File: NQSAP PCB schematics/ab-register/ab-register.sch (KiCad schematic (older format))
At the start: 56 parts, among them J1 Bus, J2 Bus, J5 Conn_02x08, J6 Conn_02x08, U1 74LS377, U2 74LS245, U3 74LS377, U4 74LS245, U5 74LS138, U6 74LS138

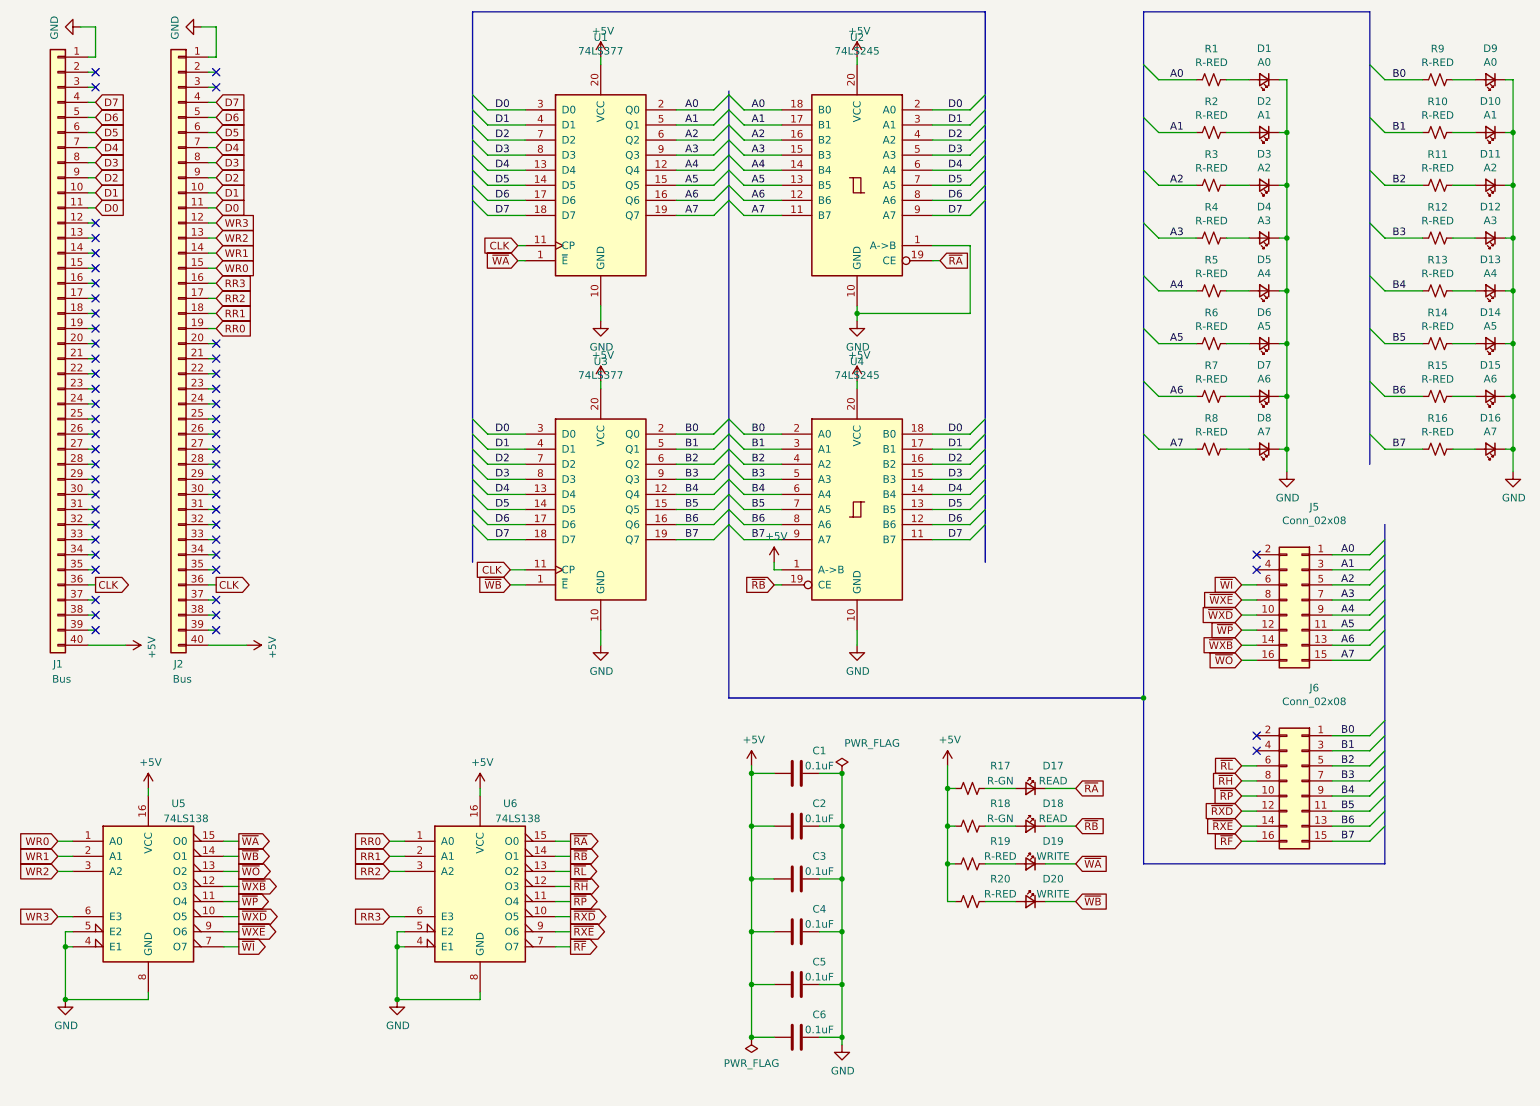
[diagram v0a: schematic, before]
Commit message: Add RAM, update and add gerbers for new boards
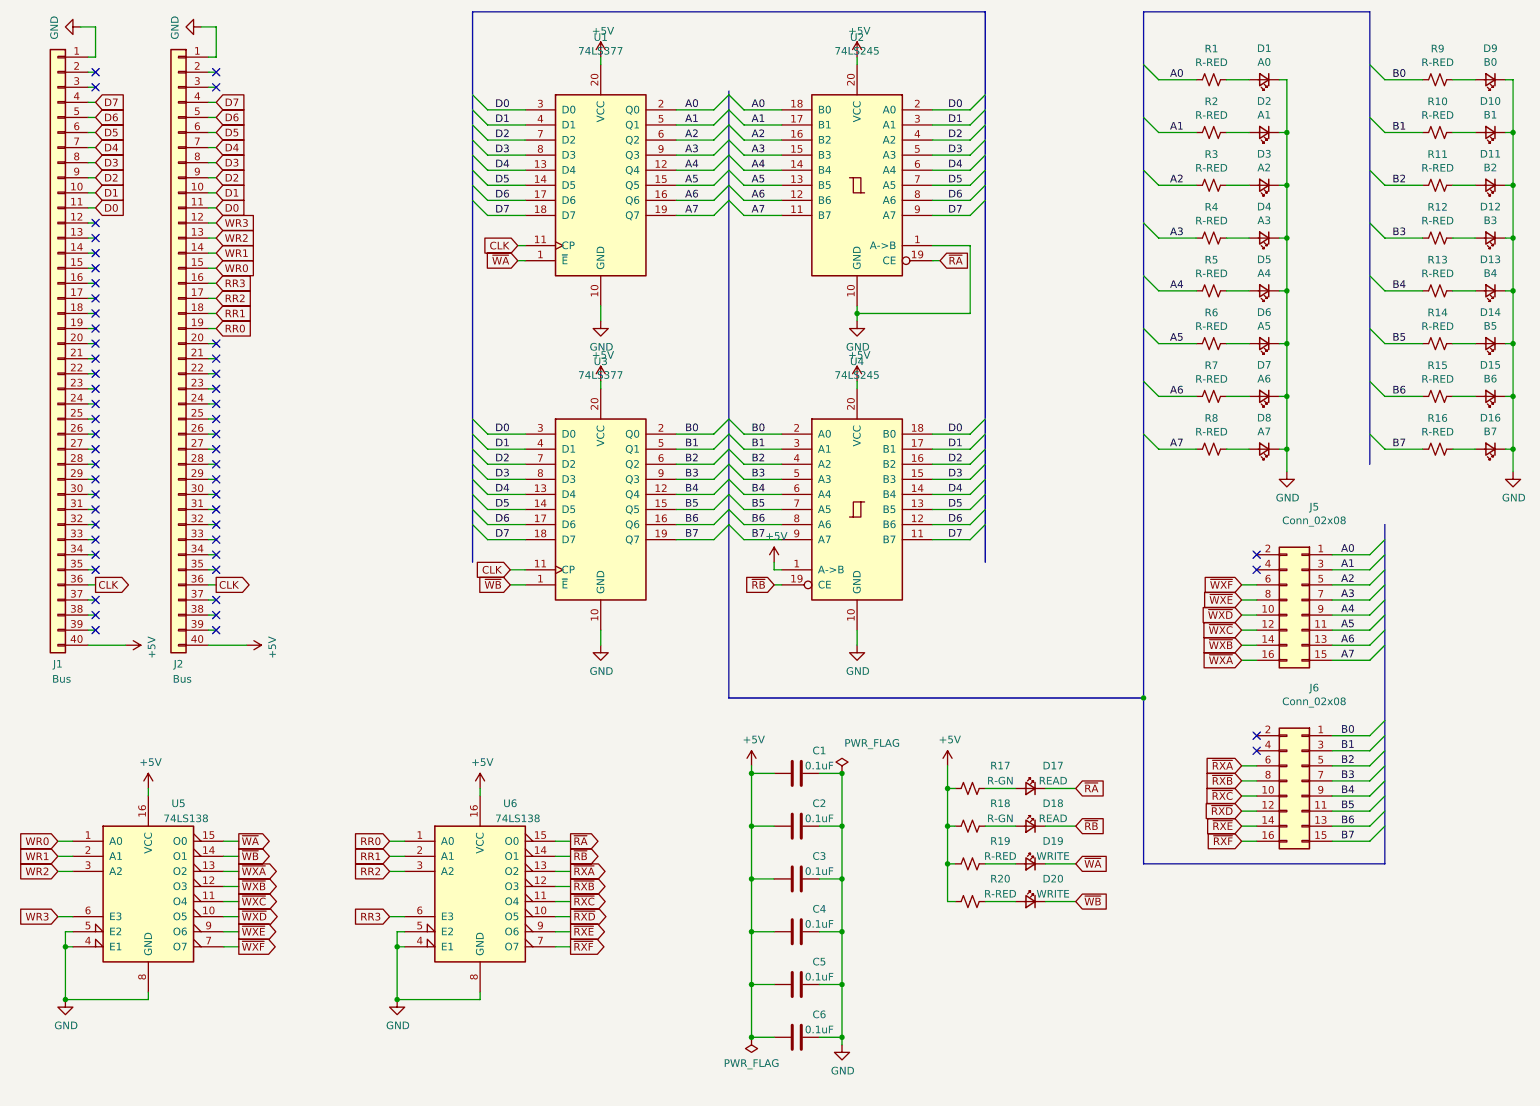
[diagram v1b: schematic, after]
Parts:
- D10: value A1 -> B1
- D11: value A2 -> B2
- D12: value A3 -> B3
- D13: value A4 -> B4
- D14: value A5 -> B5
- D15: value A6 -> B6
- D16: value A7 -> B7
- D9: value A0 -> B0
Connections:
- net ~RF renamed ~RXF
- net ~RH renamed ~RXB
- net ~RL renamed ~RXA
- net ~RP renamed ~RXC
- net ~WI renamed ~WXF
- net ~WO renamed ~WXA
- net ~WP renamed ~WXC
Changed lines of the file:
@@
 P 10300 1050
 F 0 "D9" H 10300 843 50  0000 C CNN
-F 1 "A0" H 10300 934 50  0000 C CNN
+F 1 "B0" H 10300 934 50  0000 C CNN
 F 2 "LED_SMD:LED_0805_2012Metric_Pad1.15x1.40mm_HandSolder" V 10300 1050 50  0001 C CNN
 F 3 "~" V 10300 1050 50  0001 C CNN
@@
 P 10300 1400
 F 0 "D10" H 10300 1193 50  0000 C CNN
-F 1 "A1" H 10300 1284 50  0000 C CNN
+F 1 "B1" H 10300 1284 50  0000 C CNN
 F 2 "LED_SMD:LED_0805_2012Metric_Pad1.15x1.40mm_HandSolder" V 10300 1400 50  0001 C CNN
 F 3 "~" V 10300 1400 50  0001 C CNN
@@
 P 10300 1750
 F 0 "D11" H 10300 1543 50  0000 C CNN
-F 1 "A2" H 10300 1634 50  0000 C CNN
+F 1 "B2" H 10300 1634 50  0000 C CNN
 F 2 "LED_SMD:LED_0805_2012Metric_Pad1.15x1.40mm_HandSolder" V 10300 1750 50  0001 C CNN
 F 3 "~" V 10300 1750 50  0001 C CNN
@@
 P 10300 2100
 F 0 "D12" H 10300 1893 50  0000 C CNN
-F 1 "A3" H 10300 1984 50  0000 C CNN
+F 1 "B3" H 10300 1984 50  0000 C CNN
 F 2 "LED_SMD:LED_0805_2012Metric_Pad1.15x1.40mm_HandSolder" V 10300 2100 50  0001 C CNN
 F 3 "~" V 10300 2100 50  0001 C CNN
@@
 P 10300 2450
 F 0 "D13" H 10300 2243 50  0000 C CNN
-F 1 "A4" H 10300 2334 50  0000 C CNN
+F 1 "B4" H 10300 2334 50  0000 C CNN
 F 2 "LED_SMD:LED_0805_2012Metric_Pad1.15x1.40mm_HandSolder" V 10300 2450 50  0001 C CNN
 F 3 "~" V 10300 2450 50  0001 C CNN
@@
 P 10300 2800
 F 0 "D14" H 10300 2593 50  0000 C CNN
-F 1 "A5" H 10300 2684 50  0000 C CNN
+F 1 "B5" H 10300 2684 50  0000 C CNN
 F 2 "LED_SMD:LED_0805_2012Metric_Pad1.15x1.40mm_HandSolder" V 10300 2800 50  0001 C CNN
 F 3 "~" V 10300 2800 50  0001 C CNN
@@
 P 10300 3150
 F 0 "D15" H 10300 2943 50  0000 C CNN
-F 1 "A6" H 10300 3034 50  0000 C CNN
+F 1 "B6" H 10300 3034 50  0000 C CNN
 F 2 "LED_SMD:LED_0805_2012Metric_Pad1.15x1.40mm_HandSolder" V 10300 3150 50  0001 C CNN
 F 3 "~" V 10300 3150 50  0001 C CNN
@@
 P 10300 3500
 F 0 "D16" H 10300 3293 50  0000 C CNN
-F 1 "A7" H 10300 3384 50  0000 C CNN
+F 1 "B7" H 10300 3384 50  0000 C CNN
 F 2 "LED_SMD:LED_0805_2012Metric_Pad1.15x1.40mm_HandSolder" V 10300 3500 50  0001 C CNN
 F 3 "~" V 10300 3500 50  0001 C CNN
@@
 	2000 6200 1900 6200
 Text GLabel 2000 6500 2    50   Output ~ 0
-~WP
+~WXC
 Wire Wire Line
 	2000 6500 1900 6500
@@
 	2000 6700 1900 6700
 Text GLabel 2000 6800 2    50   Output ~ 0
-~WI
+~WXF
 Wire Wire Line
 	2000 6800 1900 6800
@@
 	4200 6200 4100 6200
 Text GLabel 4200 6500 2    50   Output ~ 0
-~RP
+~RXC
 Wire Wire Line
 	4200 6500 4100 6500
@@
 	4200 6700 4100 6700
 Text GLabel 4200 6800 2    50   Output ~ 0
-~RF
+~RXF
 Wire Wire Line
 	4200 6800 4100 6800
 Text GLabel 4200 6300 2    50   Output ~ 0
-~RL
+~RXA
 Wire Wire Line
 	4200 6300 4100 6300
 Text GLabel 4200 6400 2    50   Output ~ 0
-~RH
+~RXB
 Wire Wire Line
 	4200 6400 4100 6400
@@
 ~WB
 Text GLabel 8650 4700 0    50   Input ~ 0
-~WP
+~WXC
 Wire Wire Line
 	8650 4800 8750 4800
@@
 	8650 4700 8750 4700
 Text GLabel 8650 4400 0    50   Input ~ 0
-~WI
+~WXF
 Wire Wire Line
 	8650 6000 8750 6000
@@
 ~RB
 Text GLabel 8650 5800 0    50   Input ~ 0
-~RP
+~RXC
 Wire Wire Line
 	8650 4900 8750 4900
@@
 	8650 5700 8750 5700
 Text GLabel 8650 6100 0    50   Input ~ 0
-~RF
+~RXF
 Wire Wire Line
 	8650 6100 8750 6100
 Text GLabel 8650 5600 0    50   Input ~ 0
-~RL
+~RXA
 Wire Wire Line
 	8650 5800 8750 5800
 Text GLabel 8650 5700 0    50   Input ~ 0
-~RH
+~RXB
 Wire Wire Line
 	8650 5900 8750 5900
@@
 ~WXB
 Text GLabel 2000 6300 2    50   Output ~ 0
-~WO
+~WXA
 Wire Wire Line
 	2000 6300 1900 6300
@@
 	1900 6400 2000 6400
 Text GLabel 8650 4900 0    50   Input ~ 0
-~WO
+~WXA
 Text GLabel 8650 4800 0    50   Input ~ 0
 ~WXB

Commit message: updated KiCads and gerbers for the AB Registers and IR/RC module
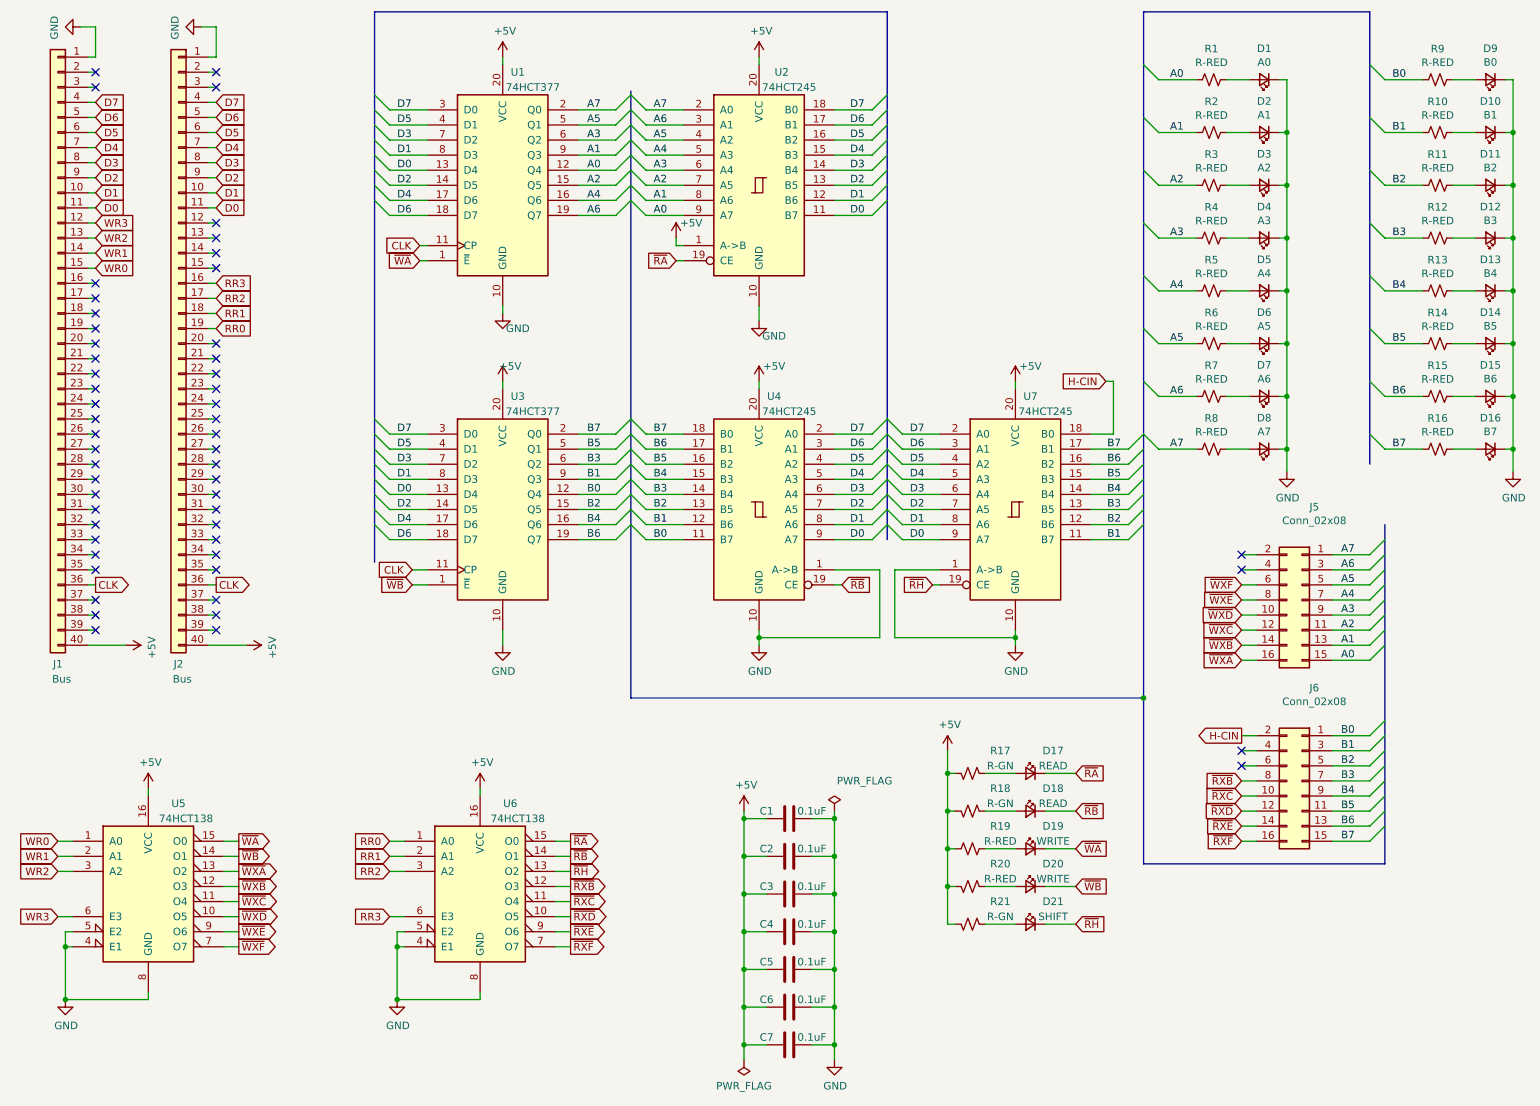
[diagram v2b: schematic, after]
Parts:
- added C7: 0.1uF, Capacitor_SMD:C_0805_2012Metric_Pad1.18x1.45mm_HandSolder, symbol Device:C
- added D21: SHIFT, LED_SMD:LED_0805_2012Metric_Pad1.15x1.40mm_HandSolder, symbol Device:LED_Small
- added R21: R-GN, Resistor_SMD:R_0805_2012Metric_Pad1.20x1.40mm_HandSolder, symbol Device:R_Small_US
- added U7: 74HCT245, Package_DIP:DIP-20_W7.62mm, symbol 74xx:74LS245
- U1, U3: value 74LS377 -> 74HCT377
- U2, U4: value 74LS245 -> 74HCT245
- U5, U6: value 74LS138 -> 74HCT138; footprint Package_SO:SOIC-16W_7.5x10.3mm_P1.27mm -> Package_DIP:DIP-16_W7.62mm
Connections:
- net +5V: now also R17.1, R18.1, R20.1, U2.1 (A->B), C7.2, R21.1, U7.20 (VCC); no longer R17.2, R18.2, R20.2, U4.1 (A->B)
- net A0: now also J5.15 (Pin_15), U1.12 (Q4), U2.9 (A7); no longer J5.1 (Pin_1), U1.2 (Q0), U2.18 (B0)
- net A1: now also J5.13 (Pin_13), U1.9 (Q3), U2.8 (A6); no longer J5.3 (Pin_3), U1.5 (Q1), U2.17 (B1)
- net A2: now also J5.11 (Pin_11), U1.15 (Q5), U2.7 (A5); no longer J5.5 (Pin_5), U1.6 (Q2), U2.16 (B2)
- net A3: now also J5.9 (Pin_9), U1.6 (Q2), U2.6 (A4); no longer J5.7 (Pin_7), U1.9 (Q3), U2.15 (B3)
- net A4: now also J5.7 (Pin_7), U1.16 (Q6), U2.5 (A3); no longer J5.9 (Pin_9), U1.12 (Q4), U2.14 (B4)
- net A5: now also J5.5 (Pin_5), U1.5 (Q1), U2.4 (A2); no longer J5.11 (Pin_11), U1.15 (Q5), U2.13 (B5)
- net A6: now also J5.3 (Pin_3), U1.19 (Q7), U2.3 (A1); no longer J5.13 (Pin_13), U1.16 (Q6), U2.12 (B6)
- net A7: now also J5.1 (Pin_1), U1.2 (Q0), U2.2 (A0); no longer J5.15 (Pin_15), U1.19 (Q7), U2.11 (B7)
- net B0: now also U3.12 (Q4), U4.11 (B7); no longer U3.2 (Q0), U4.2 (A0)
- net B1: now also U3.9 (Q3), U4.12 (B6), U7.11 (B7); no longer U3.5 (Q1), U4.3 (A1)
- net B2: now also U3.15 (Q5), U4.13 (B5), U7.12 (B6); no longer U3.6 (Q2), U4.4 (A2)
- net B3: now also U3.6 (Q2), U4.14 (B4), U7.13 (B5); no longer U3.9 (Q3), U4.5 (A3)
- net B4: now also U3.16 (Q6), U4.15 (B3), U7.14 (B4); no longer U3.12 (Q4), U4.6 (A4)
- net B5: now also U3.5 (Q1), U4.16 (B2), U7.15 (B3); no longer U3.15 (Q5), U4.7 (A5)
- net B6: now also U3.19 (Q7), U4.17 (B1), U7.16 (B2); no longer U3.16 (Q6), U4.8 (A6)
- net B7: now also U3.2 (Q0), U4.18 (B0), U7.17 (B1); no longer U3.19 (Q7), U4.9 (A7)
- net D0: now also U1.13 (D4), U2.11 (B7), U3.13 (D4), U4.9 (A7), U7.9 (A7); no longer U1.3 (D0), U2.2 (A0), U3.3 (D0), U4.18 (B0)
- net D1: now also U1.8 (D3), U2.12 (B6), U3.8 (D3), U4.8 (A6), U7.8 (A6); no longer U1.4 (D1), U2.3 (A1), U3.4 (D1), U4.17 (B1)
- net D2: now also U1.14 (D5), U2.13 (B5), U3.14 (D5), U4.7 (A5), U7.7 (A5); no longer U1.7 (D2), U2.4 (A2), U3.7 (D2), U4.16 (B2)
- net D3: now also U1.7 (D2), U2.14 (B4), U3.7 (D2), U4.6 (A4), U7.6 (A4); no longer U1.8 (D3), U2.5 (A3), U3.8 (D3), U4.15 (B3)
- net D4: now also U1.17 (D6), U2.15 (B3), U3.17 (D6), U4.5 (A3), U7.5 (A3); no longer U1.13 (D4), U2.6 (A4), U3.13 (D4), U4.14 (B4)
- net D5: now also U1.4 (D1), U2.16 (B2), U3.4 (D1), U4.4 (A2), U7.4 (A2); no longer U1.14 (D5), U2.7 (A5), U3.14 (D5), U4.13 (B5)
- net D6: now also U1.18 (D7), U2.17 (B1), U3.18 (D7), U4.3 (A1), U7.3 (A1); no longer U1.17 (D6), U2.8 (A6), U3.17 (D6), U4.12 (B6)
- net D7: now also U1.3 (D0), U2.18 (B0), U3.3 (D0), U4.2 (A0), U7.2 (A0); no longer U1.18 (D7), U2.9 (A7), U3.18 (D7), U4.11 (B7)
- net GND: now also U4.1 (A->B), C7.1, U7.1 (A->B), U7.10 (GND); no longer U2.1 (A->B)
- net WR0: now also J1.15 (Pin_15); no longer J2.15 (Pin_15)
- net WR1: now also J1.14 (Pin_14); no longer J2.14 (Pin_14)
- net WR2: now also J1.13 (Pin_13); no longer J2.13 (Pin_13)
- net WR3: now also J1.12 (Pin_12); no longer J2.12 (Pin_12)
- net H-CIN: now reaches J6.2 (Pin_2)
- net H-CIN: now also U7.18 (B0)
- net at D17.2 (A): now also R17.2; no longer R17.1
- net at D18.2 (A): now also R18.2; no longer R18.1
- net at D20.2 (A): now also R20.2; no longer R20.1
- net ~RXA: no longer names the net of J6.6 (Pin_6)
- net ~RXA: no longer U6.13 (O2)
- new net: D21.2 (A), R21.2
- new net ~RH: D21.1 (K), U6.13 (O2), U7.19 (CE)
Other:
- moved on the sheet: C1, C2, C3, C4, C5, C6, D17, D18, D19, D20, R17, R18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
